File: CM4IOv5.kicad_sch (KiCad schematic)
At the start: 0 parts

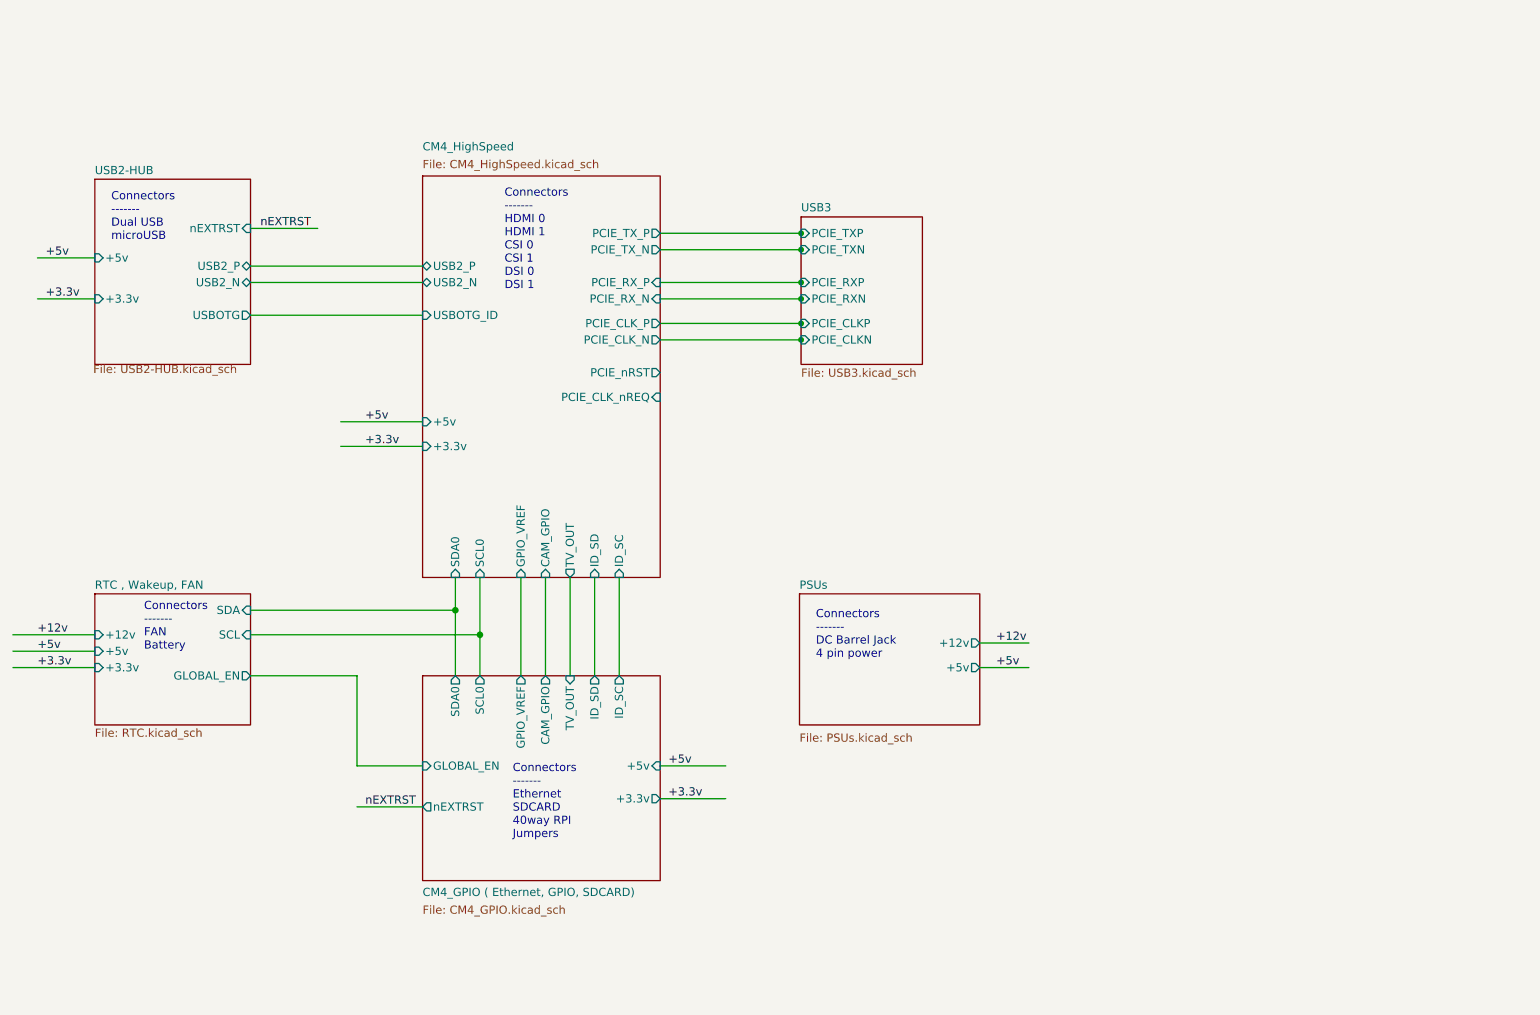
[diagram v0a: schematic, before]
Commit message: Initial layout and all parts added. Some pins still not connected to power
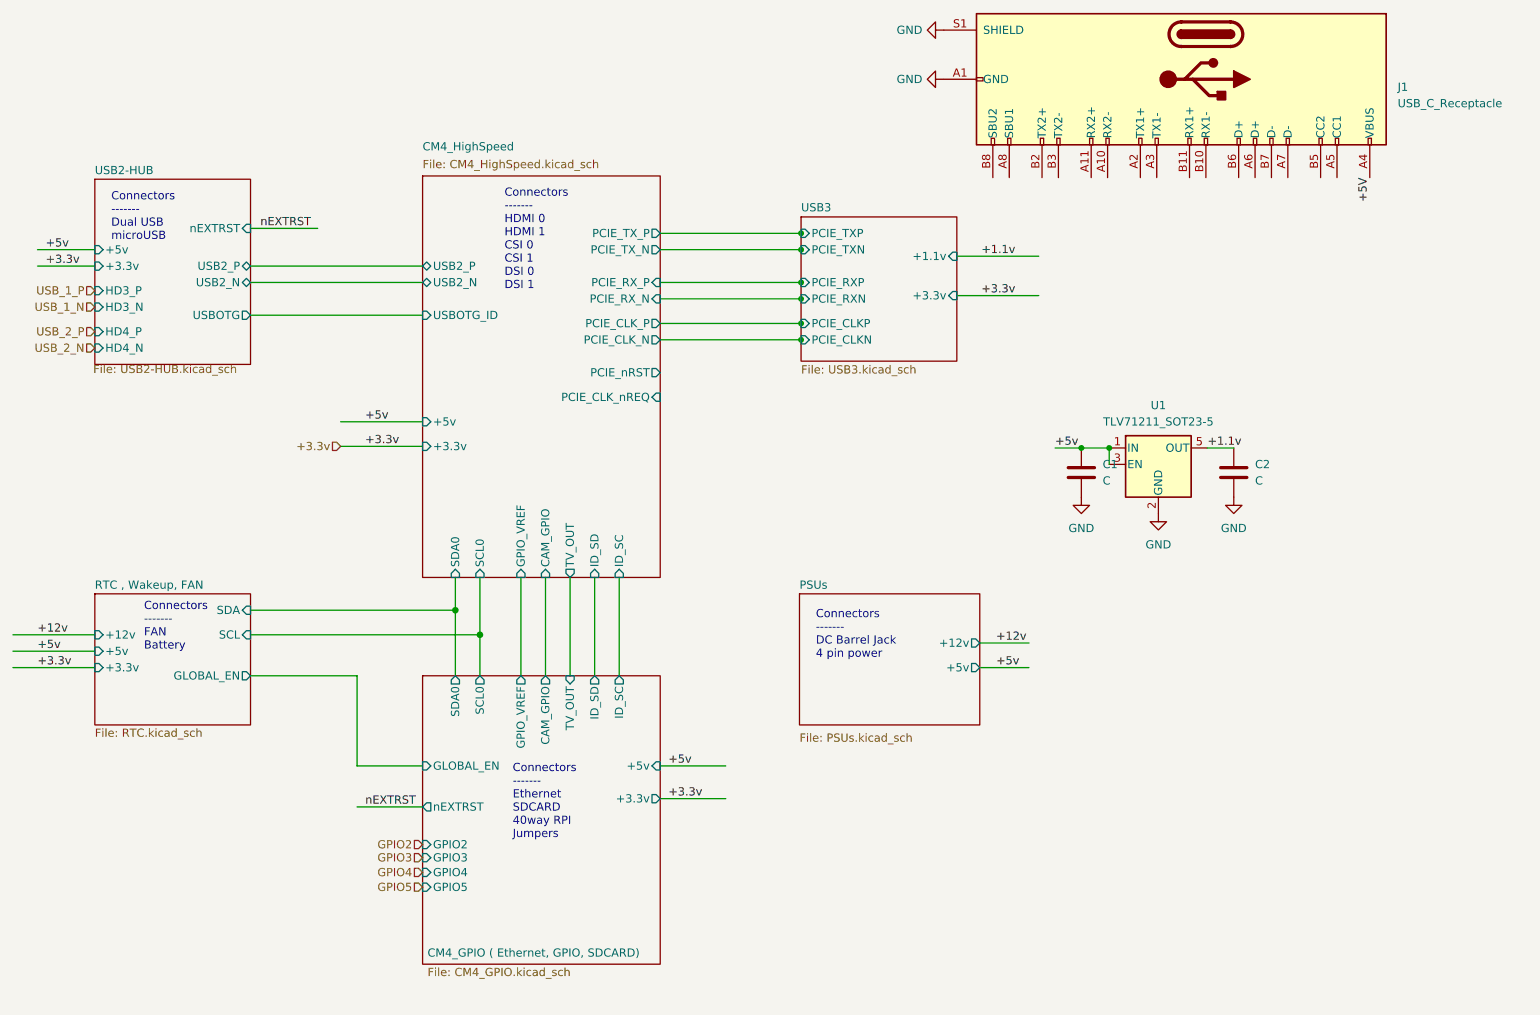
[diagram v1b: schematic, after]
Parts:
- added C1, C2: C, Capacitor_SMD:C_0402_1005Metric, symbol Device:C
- added J1: USB_C_Receptacle, Connector_USB:USB_C_Receptacle_JAE_DX07S024WJ1R350, symbol Connector:USB_C_Receptacle
- added U1: TLV71211_SOT23-5, Package_TO_SOT_SMD:SOT-23-5, symbol Regulator_Linear:TLV71211_SOT23-5
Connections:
- net +5v: now also C1.1, U1.1 (IN), U1.3 (EN)
- new net +1.1v: C2.1, U1.5 (OUT)
- new net +5V: J1.A4 (VBUS), J1.A9 (VBUS), J1.B4 (VBUS), J1.B9 (VBUS)
- new net GND: C1.2, C2.2, J1.A1 (GND), J1.A12 (GND), J1.B1 (GND), J1.B12 (GND), J1.S1 (SHIELD), U1.2 (GND)
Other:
- sheet CM4_GPIO ( Ethernet, GPIO, SDCARD) ports: added GPIO2, GPIO3, GPIO4, GPIO5; removed none
- sheet USB2-HUB ports: added HD3_N, HD3_P, HD4_N, HD4_P; removed none
- sheet USB3 ports: added +1.1v, +3.3v; removed none

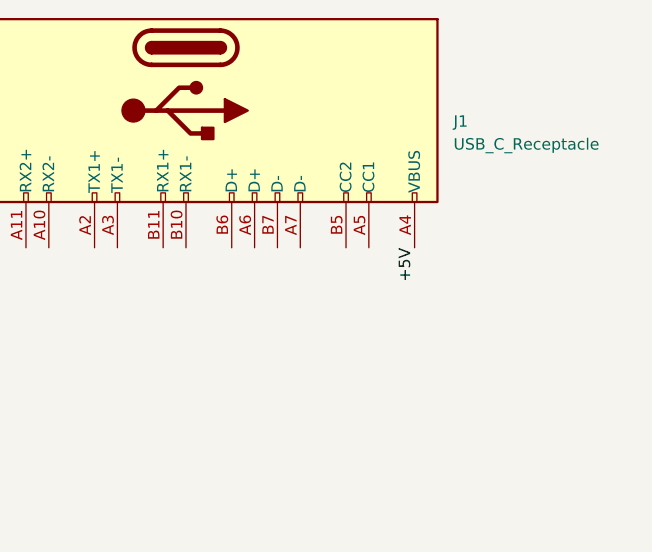
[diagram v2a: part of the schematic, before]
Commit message: mostly routed, need to add more layers fo power and finish low speed signal routing
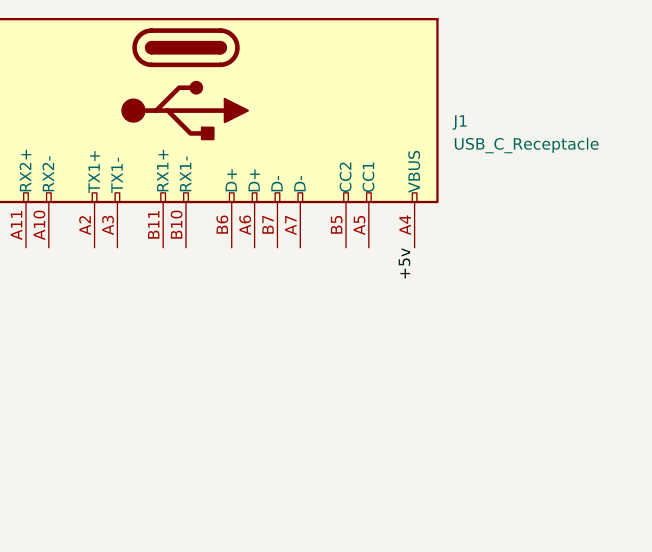
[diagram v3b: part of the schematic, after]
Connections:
- net +5V is gone; now on net +5v: J1.A4 (VBUS), J1.A9 (VBUS), J1.B4 (VBUS), J1.B9 (VBUS)
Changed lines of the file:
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@@
   (junction (at 190.7441 62.23) (diameter 0) (color 0 0 0 0))
   (junction (at 140.97 110.49) (diameter 1.016) (color 0 0 0 0))
+  (junction (at 137.16 106.68) (diameter 1.016) (color 0 0 0 0))
+  (junction (at 190.7441 55.88) (diameter 0) (color 0 0 0 0))
   (junction (at 238.506 81.534) (diameter 0) (color 0 0 0 0))
   (junction (at 190.7441 50.8) (diameter 0) (color 0 0 0 0))
-  (junction (at 137.16 106.68) (diameter 1.016) (color 0 0 0 0))
+  (junction (at 190.7441 58.42) (diameter 0) (color 0 0 0 0))
   (junction (at 190.7441 64.77) (diameter 0) (color 0 0 0 0))
-  (junction (at 190.7441 58.42) (diameter 0) (color 0 0 0 0))
-  (junction (at 190.7441 55.88) (diameter 0) (color 0 0 0 0))
   (wire (pts (xy 68.58 113.03) (xy 81.28 113.03))
     (stroke (width 0) (type solid) (color 0 0 0 0))
@@
     (stroke (width 0) (type solid) (color 0 0 0 0))
   )
-  (wire (pts (xy 230.124 81.534) (xy 234.188 81.534))
+  (wire (pts (xy 234.188 81.534) (xy 238.506 81.534))
     (stroke (width 0) (type default) (color 0 0 0 0))
   )
-  (wire (pts (xy 234.188 81.534) (xy 238.506 81.534))
+  (wire (pts (xy 230.124 81.534) (xy 234.188 81.534))
     (stroke (width 0) (type default) (color 0 0 0 0))
   )
@@
     (stroke (width 0) (type solid) (color 0 0 0 0))
   )
-  (wire (pts (xy 168.91 58.42) (xy 190.7441 58.42))
+  (wire (pts (xy 190.7441 58.42) (xy 190.754 58.42))
     (stroke (width 0) (type default) (color 0 0 0 0))
   )
-  (wire (pts (xy 190.7441 58.42) (xy 190.754 58.42))
+  (wire (pts (xy 168.91 58.42) (xy 190.7441 58.42))
     (stroke (width 0) (type default) (color 0 0 0 0))
   )
@@
     (effects (font (size 1.27 1.27)) (justify left bottom))
   )
-  (label "+5V" (at 278.892 39.624 270)
+  (label "+5v" (at 278.892 39.624 270)
     (effects (font (size 1.27 1.27)) (justify right bottom))
   )

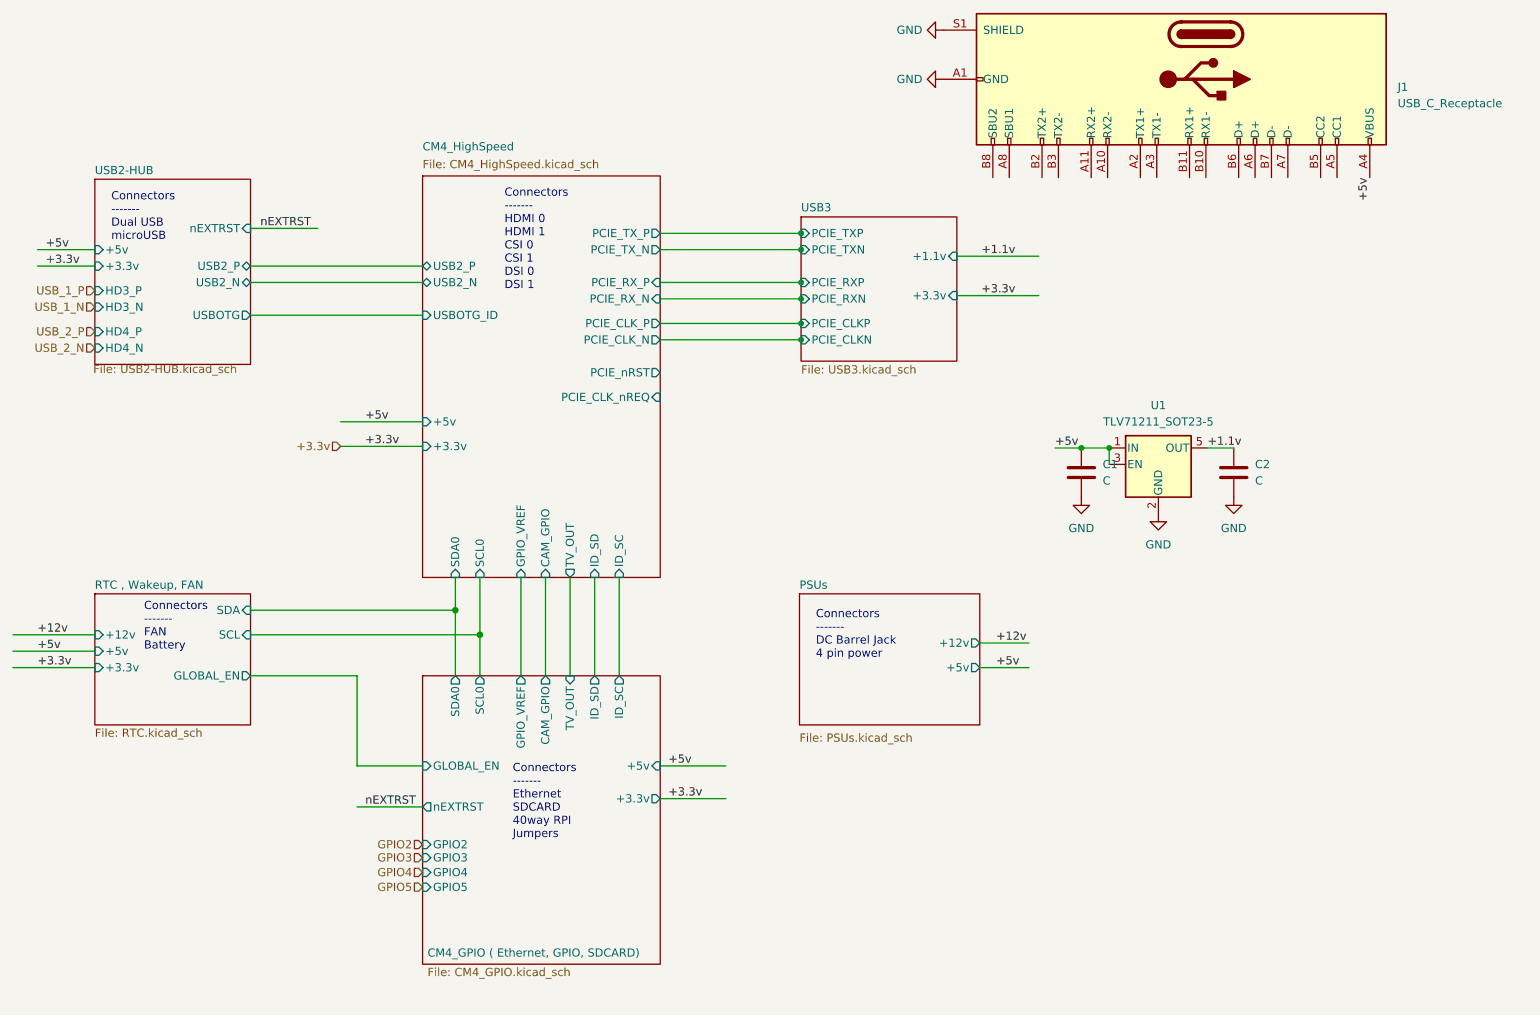
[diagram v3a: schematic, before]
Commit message: Added usb to ethernet and changed mcu to stm32g4
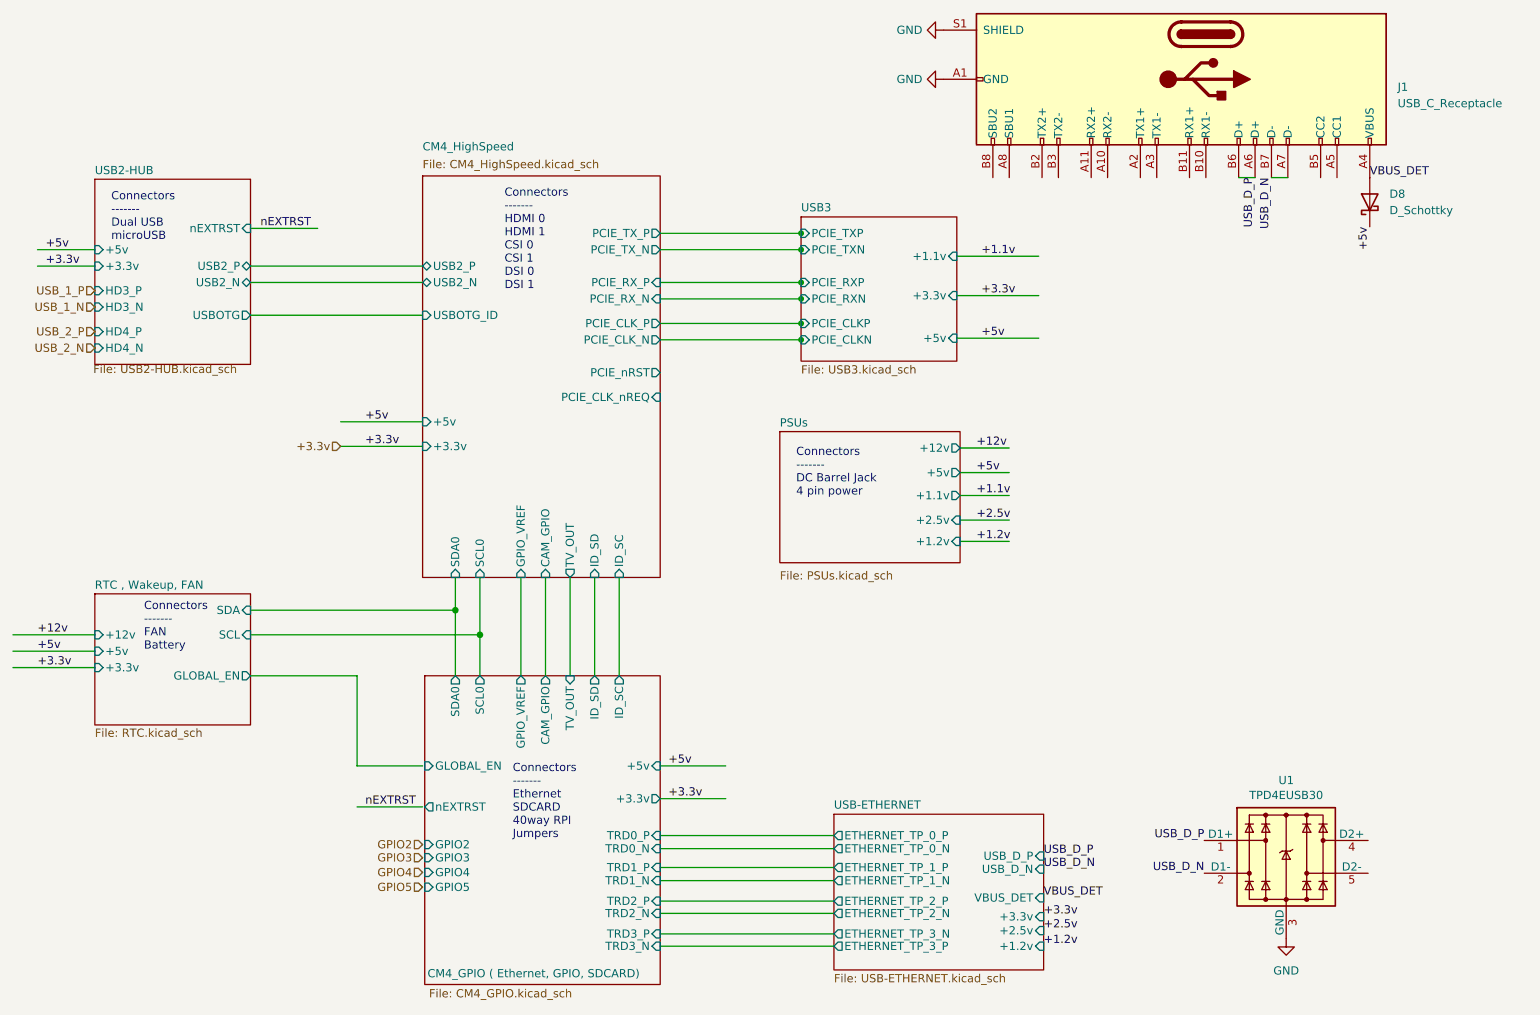
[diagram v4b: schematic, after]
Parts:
- removed C1, C2: C, Capacitor_SMD:C_0402_1005Metric, symbol Device:C
- removed U1: TLV71211_SOT23-5, Package_TO_SOT_SMD:SOT-23-5, symbol Regulator_Linear:TLV71211_SOT23-5
- added D8: D_Schottky, Diode_SMD:D_1210_3225Metric, symbol Device:D_Schottky
- added U1: TPD4EUSB30, Package_SON:USON-10_2.5x1.0mm_P0.5mm, symbol CM4IO:TPD4EUSB30
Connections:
- net +5v: now also D8.1 (K); no longer J1.A4 (VBUS), J1.A9 (VBUS), J1.B4 (VBUS), J1.B9 (VBUS)
- net GND: now also U1.3 (GND), U1.8 (GND)
- net USB_D_P: now reaches J1.A6 (D+)
- net USB_D_P: now also J1.B6 (D+), U1.1 (D1+), U1.10
- net USB_D_N: now reaches J1.A7 (D-)
- net USB_D_N: now also J1.B7 (D-), U1.2 (D1-), U1.9
- new net: U1.4 (D2+), U1.7
- new net: U1.5 (D2-), U1.6
- new net VBUS_DET: D8.2 (A), J1.A4 (VBUS), J1.A9 (VBUS), J1.B4 (VBUS), J1.B9 (VBUS)
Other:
- added sheet USB-ETHERNET (USB-ETHERNET.kicad_sch)
- sheet CM4_GPIO ( Ethernet, GPIO, SDCARD) ports: added TRD0_N, TRD0_P, TRD1_N, TRD1_P, TRD2_N, TRD2_P, TRD3_N, TRD3_P; removed none
- sheet PSUs ports: added +1.1v, +1.2v, +2.5v; removed none
- sheet USB3 ports: added +5v; removed none
